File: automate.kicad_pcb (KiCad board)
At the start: 4 copper layers, 196.8 x 136.2 mm, 240 parts, among them J1 Conn_01x02_Female, J10 Conn_01x03_Female, J11 Conn_01x03_Female, J12 Conn_01x03_Female, J13 Conn_01x02_Female, J14 Conn_01x02_Female, J15 Conn_01x02_Female, J16 Conn_01x02_Female, J17 Conn_01x02_Female, J18 Conn_01x02_Female, J19 Conn_01x02_Female, J2 Conn_01x06_Female, J20 Conn_01x02_Female, J21 Conn_01x02_Female, J22 Conn_01x02_Female, J23 Conn_01x02_Female, J24 Conn_01x02_Female, J25 Conn_01x05_Female, J26 Conn_01x05_Female, J27 Conn_01x02_Female, J3 Conn_01x04_Female, J4 Conn_01x04_Female, J5 Conn_01x03_Female, J6 Conn_01x03_Female, J7 Conn_01x03_Female, J8 Conn_01x03_Female, J9 Conn_01x03_Female, K1 SONGLE, K2 SONGLE, K3 SONGLE, K4 SONGLE, K5 SONGLE, K6 SONGLE, K7 SONGLE, K8 SONGLE, Q1 BC817, Q10 BC817, Q11 BC817, Q12 BC817, Q13 BC817, Q14 BC817, Q15 BC817, Q16 BC817, Q17 BC817, Q2 BC817, Q3 BC817, Q4 BC817, Q5 BC817, Q6 BC817, Q7 BC817, Q8 BC817, Q9 BC817, SW1 SW_Push, U1 LT1376CS8TR, U2 PIC16F1939-PDIP40

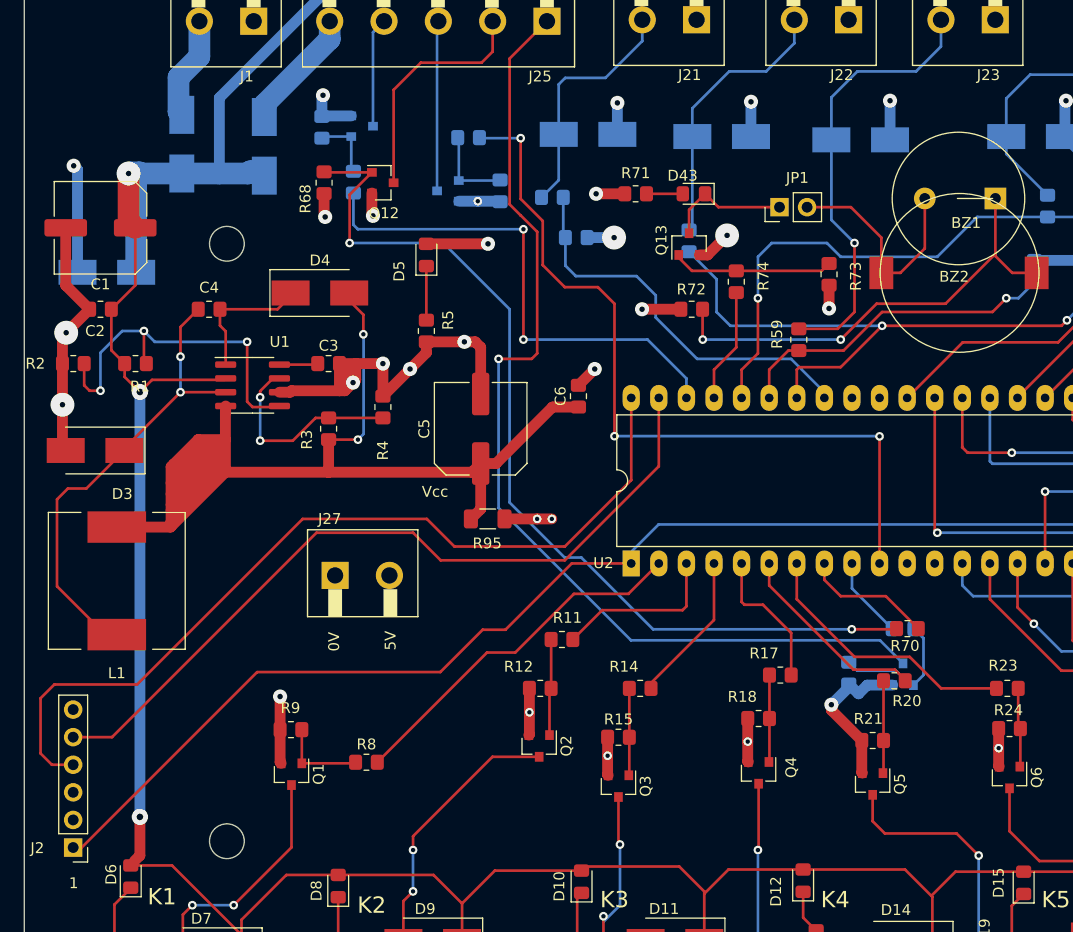
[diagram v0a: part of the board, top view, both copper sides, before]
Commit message: modification position L1, correction sérigraphie
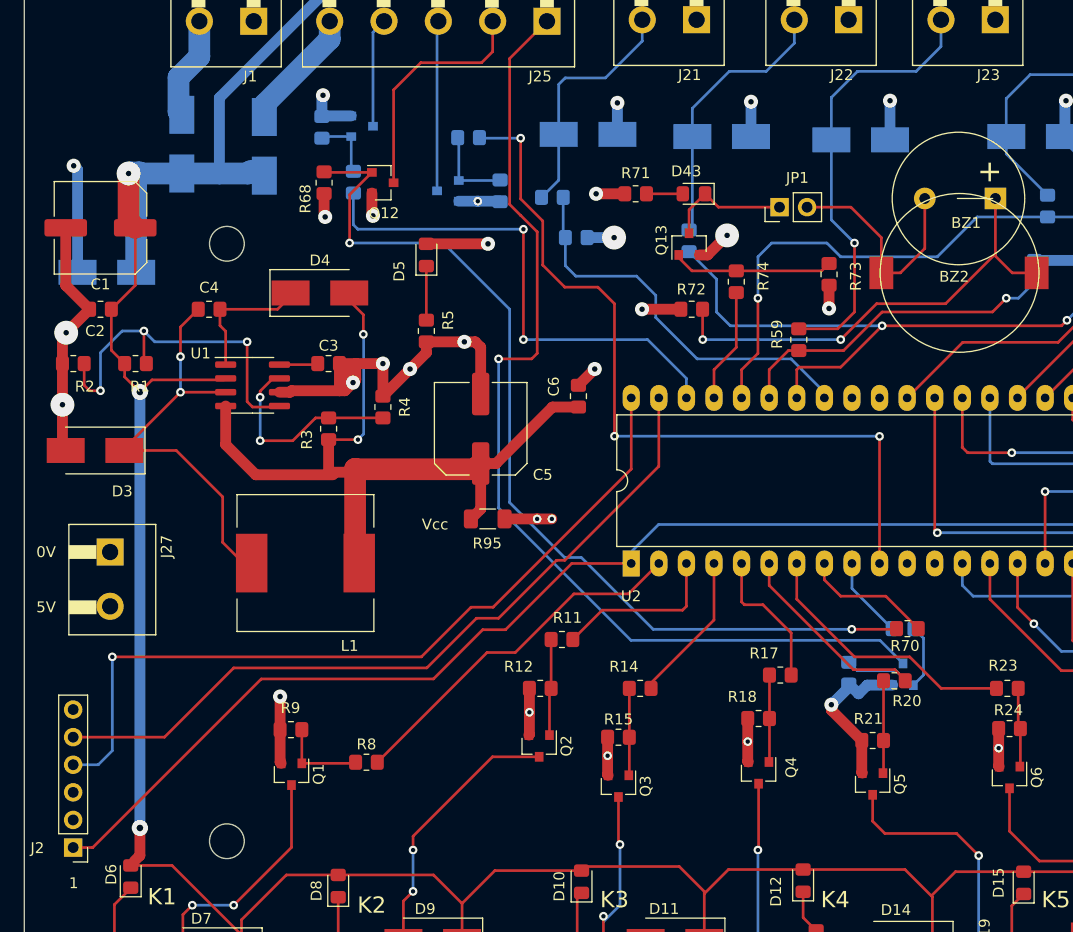
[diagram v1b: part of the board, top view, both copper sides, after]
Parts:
- moved J27 20.8 mm to (57.2, 91.9), turned to -90 degrees
- moved L1 17.4 mm to (75.2, 93.0), turned to 0 degrees
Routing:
- net Net-(C5-Pad1): track 121.1 -> 84.4 mm
- net Net-(J2-Pad4): track 80.9 -> 74.3 mm, vias 0 -> 1
- net Net-(C4-Pad2): track 42.1 -> 37.5 mm
- net Net-(J2-Pad5): track 72.6 -> 70.5 mm
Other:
- board text added: "+"
